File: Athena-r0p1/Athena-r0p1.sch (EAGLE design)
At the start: 30 parts, among them U1 3.3V, U2 AP2127K-1.8V, U3 NCP1117LPST50T3G

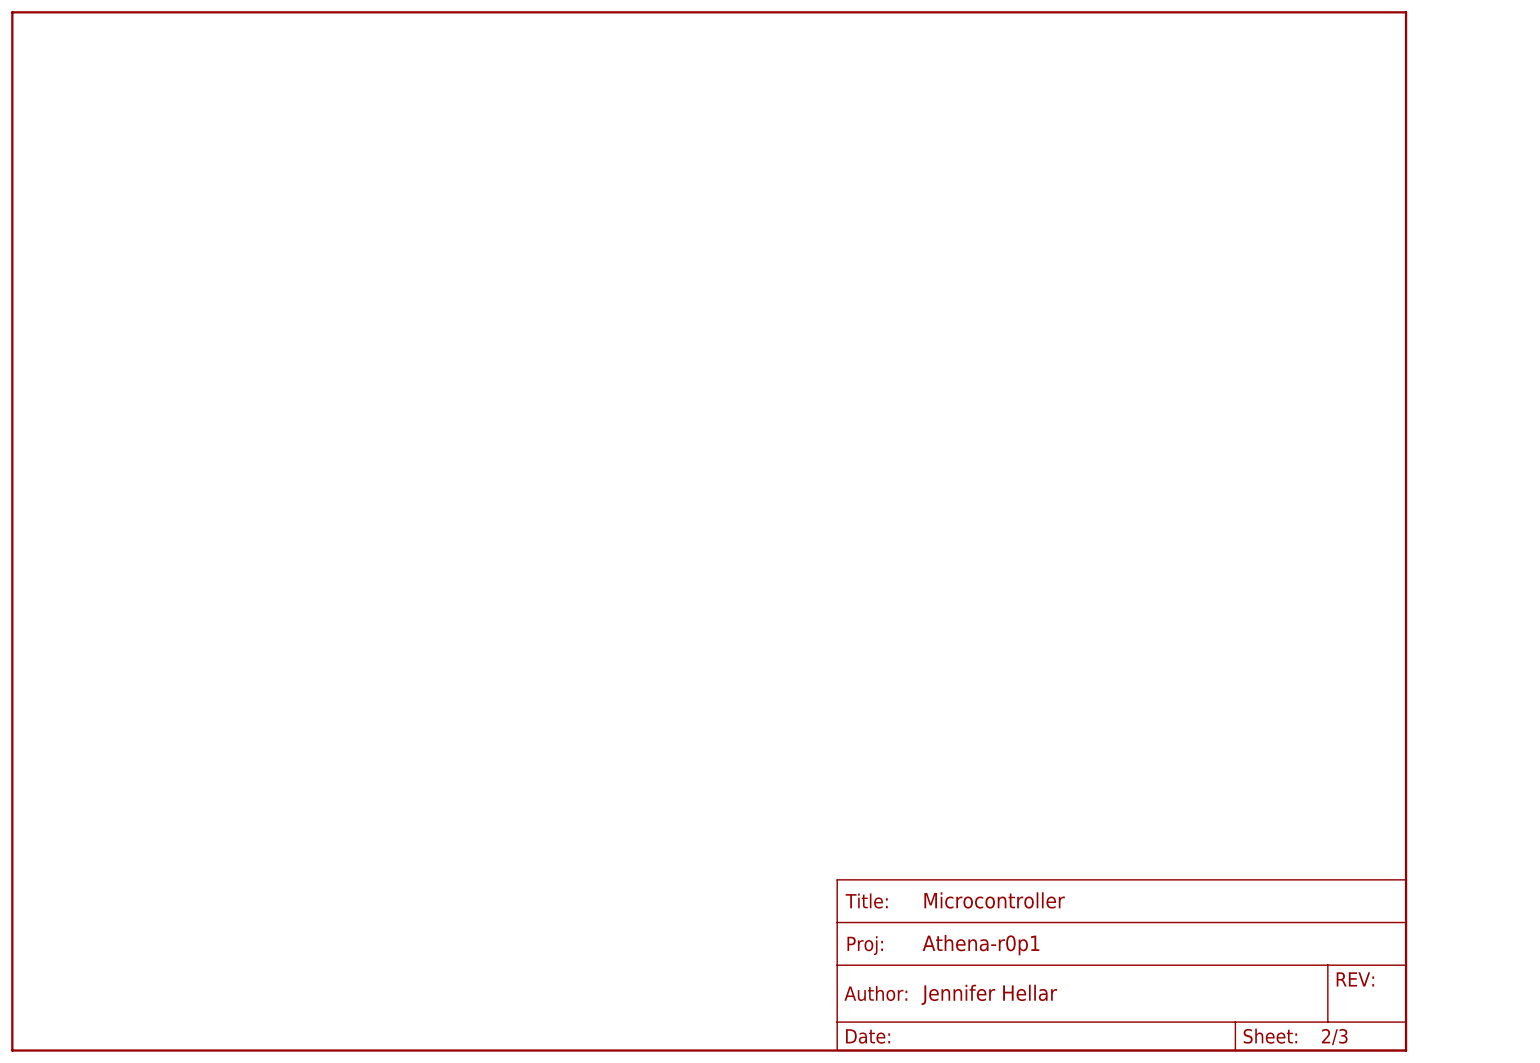
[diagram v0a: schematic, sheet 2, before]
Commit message: Initial work on the MCU portion of the schematic incl. oscillators and flash
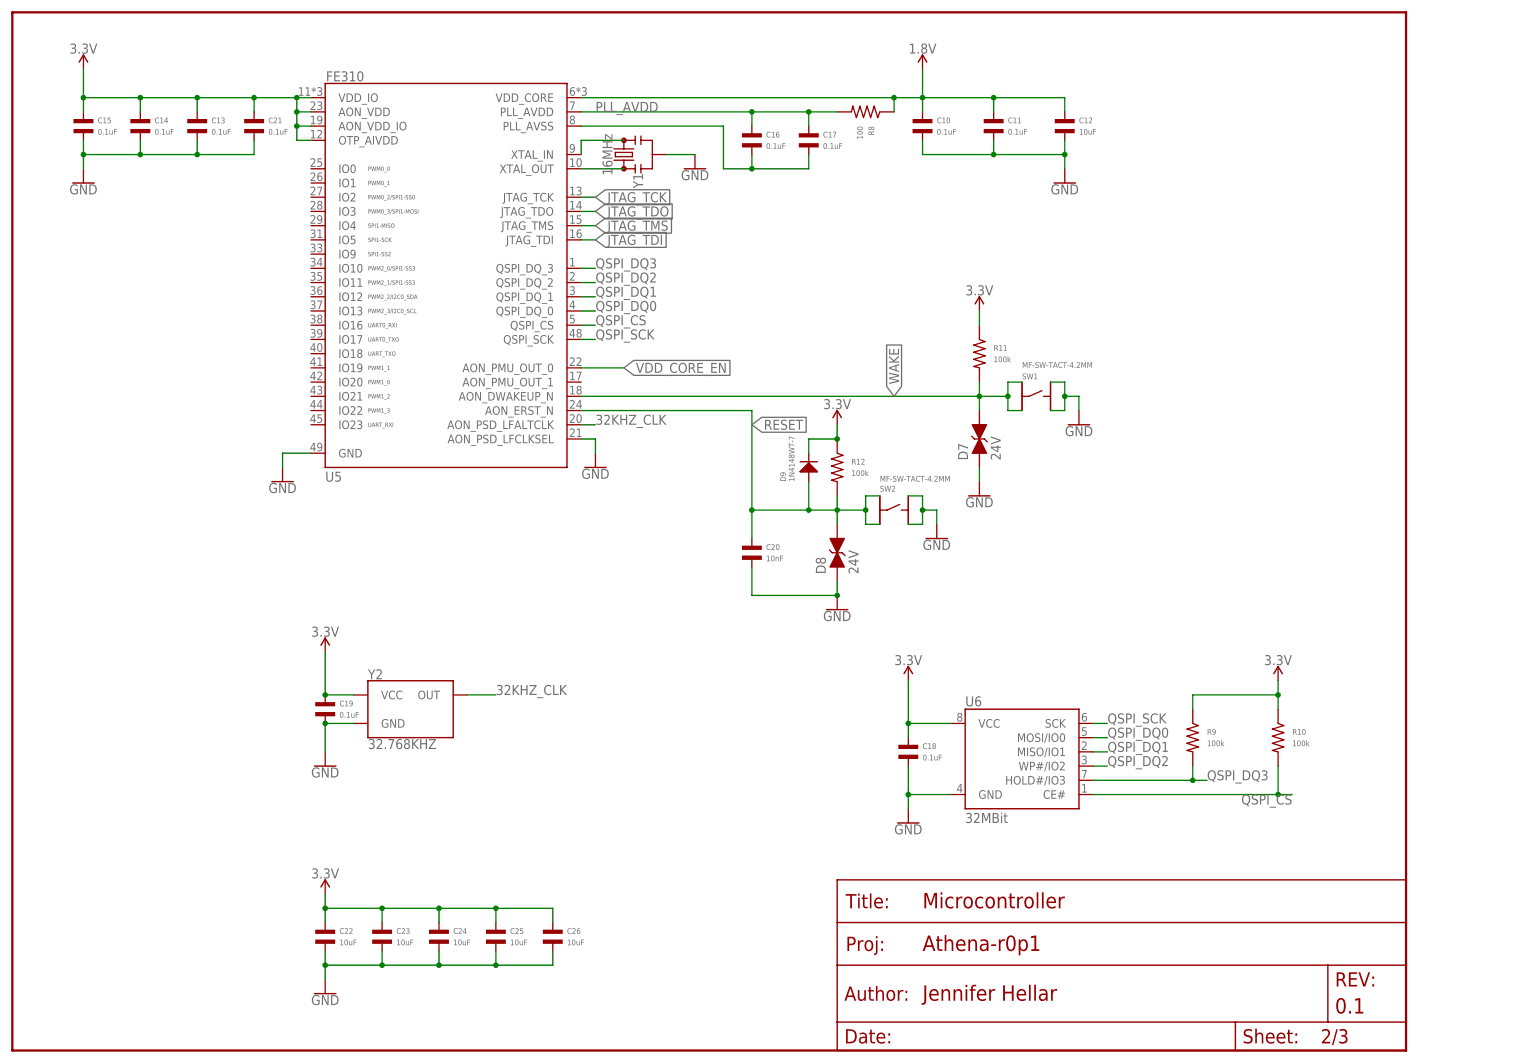
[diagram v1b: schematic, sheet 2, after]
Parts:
- added C10, C11, C13, C14, C15, C16, C17, C18, C19, C21: 0.1uF, MF_Passives:CAPACITOR_NP_0603
- added C12, C22, C23, C24, C25, C26: 10uF, MF_Passives:CAPACITOR_NP_0603
- added C20: 10nF, MF_Passives:CAPACITOR_NP_0603
- added D7, D8: 24V, SparkFun RED-V RedBoard:SPARKFUN-DISCRETESEMI_DIODE_TVS
- added D9: 1N4148WT-7, Athena-r0p1:1N4148WT-7
- added R10, R11, R12, R9: 100k, MF_Passives:RESISTOR_0603
- added R13, R14, R15, R8: 100, MF_Passives:RESISTOR_0603
- added SW1, SW2: MF-SW-TACT-4.2MM, MF_Switches:TACT_4.2MM
- added U5: FE310, Athena-r0p1:IC_MCU_SIFIVE_FE310
- added U6: 32MBit, Athena-r0p1:IC_MEMORY_QSPI32MBIT
- added U7: MK22FN128VLH10, Athena-r0p1:IC_USB_JTAG_MK22FN128VLH10
- added Y1: 16MHz, Athena-r0p1:CLOCK_16MHZ_RESONATORSMD_3.2X1.3
- added Y2: 32.768KHZ, Athena-r0p1:CLOCK_SITIME_CRYSTAL_32.768KHZ
- FRAME1, FRAME2: REV (none) -> 0.1
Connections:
- new net 32KHZ_CLK: U5.AON_PSD_LFALTCLK, Y2.OUT
- new net JTAG_TCK: R14.P$2, U5.JTAG_TCK
- new net JTAG_TDI: R13.P$2, U5.JTAG_TDI
- new net JTAG_TDO: U5.JTAG_TDO, U7.PTE1/LLWU_P0
- new net JTAG_TMS: R15.P$1, U5.JTAG_TMS
- new net N$10: C16.P$2, C17.P$2, U5.PLL_AVSS
- new net N$11: U5.XTAL_OUT, Y1.1
- new net N$12: R13.P$1, U7.PTD2/LLWU_P13
- new net N$14: R14.P$1, U7.PTD5
- new net N$16: R15.P$2, U7.PTD6/LLWU_P15
- new net N$9: U5.XTAL_IN, Y1.3
- new net PLL_AVDD: C16.P$1, C17.P$1, R8.P$2, U5.PLL_AVDD
- new net QSPI_CS: R10.P$2, U5.QSPI_CS, U6.CE#
- new net QSPI_DQ0: U5.QSPI_DQ_0, U6.MOSI/IO0
- new net QSPI_DQ1: U5.QSPI_DQ_1, U6.MISO/IO1
- new net QSPI_DQ2: U5.QSPI_DQ_2, U6.WP#/IO2
- new net QSPI_DQ3: R9.P$2, U5.QSPI_DQ_3, U6.HOLD#/IO3
- new net QSPI_SCK: U5.QSPI_SCK, U6.SCK
- new net RESET: C20.P$1, D8.C, D9.ANODE, R12.P$2, SW2.P$3, SW2.P$4, U5.AON_ERST_N
- new net WAKE: D7.C, R11.P$2, SW1.P$3, SW1.P$4, U5.AON_DWAKEUP_N
- net 1.8V: now also C10.P$1, C11.P$1, C12.P$1, R8.P$1, U5.VDD_CORE
- net 3.3V: now also C13.P$1, C14.P$1, C15.P$1, C18.P$1, C19.P$1, C21.P$1, C22.P$1, C23.P$1, C24.P$1, C25.P$1, C26.P$1, D9.CATHODE, R10.P$1, R11.P$1, R12.P$1, R9.P$1, U5.AON_VDD, U5.AON_VDD_IO, U5.OTP_AIVDD, U5.VDD_IO, U6.VCC, Y2.VCC; no longer C1.P$2, C4.P$2, C5.P$2, C6.P$2, C8.P$2, C9.P$2, D2.CATHODE, D3.CATHODE, D4.CATHODE, R6.P$1, U1.GND, U2.GND, U4.VSS, X1.2
- net GND: now also C1.P$2, C10.P$2, C11.P$2, C12.P$2, C13.P$2, C14.P$2, C15.P$2, C18.P$2, C19.P$2, C20.P$2, C21.P$2, C22.P$2, C23.P$2, C24.P$2, C25.P$2, C26.P$2, C4.P$2, C5.P$2, C6.P$2, C8.P$2, C9.P$2, D2.CATHODE, D3.CATHODE, D4.CATHODE, D7.A, D8.A, R6.P$1, SW1.P$1, SW1.P$2, SW2.P$1, SW2.P$2, U1.GND, U2.GND, U4.VSS, U5.AON_PSD_LFCLKSEL, U5.GND, U6.GND, X1.2, Y1.2, Y2.GND
- net VDD_CORE_EN: now also U5.AON_PMU_OUT_0

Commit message: Initial work on the USB-JTAG portion of Nest.  Added PWR/JTAG header to separate Owl and Nest.  Pdf of RedBoard schematic reference added for ease of viewing
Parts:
- added C27, C28, C29, C30, C32: 0.1uF, MF_Passives:CAPACITOR_NP_0603
- added C31: 10uF, MF_Passives:CAPACITOR_NP_0603
- added FRAME4: FRAME-LETTER, Athena-r0p1:FRAME-LETTER
- added J1: CONN_12X2, SparkFun-Connectors:CONN_12X2
- added J2: MF-CON-MICROUSB-RIGHT, MF_Connectors:USB_MICRO_RIGHT
- added J3-MK22-DBG: FEMALE 2x3, SparkFun-Connectors:CONN_03X2FEMALE
- added R16: 100k, MF_Passives:RESISTOR_0603
- added U8: MIC803-30D2VC3-TR, Athena-r0p1:MIC803-30D2VC3-TR
- FRAME1: SHEETNM Power -> Power (Nest)
- FRAME2: SHEETNM Microcontroller -> Microcontroller (Owl)
- FRAME3: REV (none) -> 0.1; SHEETNM Nest -> USB-JTAG (Nest)
- U1: value 3.3V -> NCP1117-VREG-5V0; device Athena-r0p1:IC_POWER_3.3V_REG_AP2112K-3.3V -> Athena-r0p1:NCP1117LPST50T3G
- U2: value AP2127K-1.8V -> AP2112-VREG-3V3; device Athena-r0p1:IC_POWER_1P8V_REG_AP2127K-1.8V -> Athena-r0p1:IC_POWER_3.3V_REG_AP2112K-3.3V
- U3: value NCP1117LPST50T3G -> AP2127K-VREG-1V8; device Athena-r0p1:NCP1117LPST50T3G -> Athena-r0p1:IC_POWER_1P8V_REG_AP2127K-1.8V
- U4: value (none) -> MCP73831/2
- X1: value (none) -> JST 2-Pin
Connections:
- new net CORE_EN_NEST: J1.24, R2.P$2, R5.P$1
- new net DBG_RESET: J3-MK22-DBG.3, R16.P$1, U7.RESET_B, U8.!RESET
- new net DBG_SWDCLK: J3-MK22-DBG.4, U7.PTA0
- new net DBG_SWDIO: J3-MK22-DBG.2, U7.PTA3
- new net DBG_SWO: J3-MK22-DBG.6, U7.PTA2
- new net JTAG_TCK_NEST: J1.16, R14.P$2
- new net JTAG_TDI_NEST: J1.20, R13.P$2
- new net JTAG_TDO_NEST: J1.18, U7.PTE1/LLWU_P0
- new net JTAG_TMS_NEST: J1.14, R15.P$1
- new net RESET_NEST: J1.22, U7.PTD7
- new net UART_RX: J1.11, U5.IO16
- new net UART_RX_NEST: J1.10, U7.PTB16
- new net UART_TX: J1.9, U5.IO17
- new net UART_TX_NEST: J1.12, U7.PTB17
- new net USB_N: J2.D-, U7.D-
- new net USB_P: J2.D+, U7.D+
- net 1.8V: now also J1.7, J1.8, U3.OUT; no longer U2.OUT
- net 3.3V: now also C27.P$1, C28.P$1, C29.P$1, C30.P$1, C31.P$1, D2.ANODE, J1.5, J1.6, J3-MK22-DBG.1, R16.P$2, U2.OUT, U7.PTA4/LLWU_P3, U7.USBVDD, U7.VBATT, U7.VDD, U7.VDDA, U7.VREFH; no longer R3.P$1, U1.OUT
- net 5V: now also C32.P$1, J1.3, J1.4, U1.OUTPUT, U3.IN, U8.VCC; no longer U1.IN, U3.OUTPUT
- net GND: now also C27.P$2, C28.P$2, C29.P$2, C30.P$2, C31.P$2, C32.P$2, J1.1, J1.2, J2.GND, J2.SLD, J3-MK22-DBG.5, R3.P$2, U1.ADJUST/GROUND, U3.GND, U7.GND, U7.VREFL, U7.VSSA, U8.GND; no longer D2.CATHODE, U1.GND, U3.ADJUST/GROUND
- net JTAG_TCK: now also J1.15; no longer R14.P$2
- net JTAG_TDI: now also J1.19; no longer R13.P$2
- net JTAG_TDO: now also J1.17; no longer U7.PTE1/LLWU_P0
- net JTAG_TMS: now also J1.13; no longer R15.P$1
- net N$2: now also D2.CATHODE, R3.P$1; no longer D2.ANODE, R3.P$2
- net N$3: now also U2.EN; no longer U1.EN
- net N$4: now also U3.EN; no longer U2.EN
- net RESET: now also J1.21
- net VDD_CORE_EN: now also J1.23; no longer R2.P$2, R5.P$1
- net V_USB: now also J2.5V, U1.INPUT; no longer U3.INPUT
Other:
- note added: "Is one pin sufficient for transferring pwr from nest to owl? Or should we double up 3.3V and 1.8V and GND pins to have a stronger connection?"
- note added: "Not sure how to incorporate multiple power sources (V_BATT and V_USB) Also need to choose an actual device for D6"
- note added: "Resistor(s) needed for impedance matching?"

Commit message: Athena Rev. 0.1 Schematic complete.
1. Switched out oscillators to match the parts used in HiFive
2. Cleaned and commented the schematics
3. Completed the header pinout
4. Removed unused parts from the library
5. Added datasheets for all non-passives
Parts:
- removed J1: CONN_12X2, SparkFun-Connectors:CONN_12X2
- removed J2: MF-CON-MICROUSB-RIGHT, MF_Connectors:USB_MICRO_RIGHT
- added C33, C34: 15pF, MF_Passives:CAPACITOR_NP_0603
- added FRAME5: FRAME-LETTER, Athena-r0p1:FRAME-LETTER
- added J1-NEST-OWL1: CONN_12X2, SparkFun-Connectors:CONN_12X2
- added J2-USB: MF-CON-MICROUSB-RIGHT, MF_Connectors:USB_MICRO_RIGHT
- added J4, J5: MF-CON-2.54mm-01x14, MF_Connectors:CON_01X14_PTH_2.54MM
- added R17: 1M, MF_Passives:RESISTOR_0603
- D6: value (none) -> MBR120
- U2: value AP2112-VREG-3V3 -> RT9080-33GJ5; device Athena-r0p1:IC_POWER_3.3V_REG_AP2112K-3.3V -> Athena-r0p1:RT9080-33GJ5
- U3: value AP2127K-VREG-1V8 -> RT9080-18GJ5; device Athena-r0p1:IC_POWER_1P8V_REG_AP2127K-1.8V -> Athena-r0p1:RT9080-18GJ5
- Y1: value 16MHz -> TSX-3225-16.0000MF18X-AC0; device Athena-r0p1:CLOCK_16MHZ_RESONATORSMD_3.2X1.3 -> Athena-r0p1:TSX-3225-16.0000MF18X-AC0
- Y2: value 32.768KHZ -> SIT1533AI-H4-DCC-32.768E; device Athena-r0p1:CLOCK_SITIME_CRYSTAL_32.768KHZ -> Athena-r0p1:SIT1533AI-H4-DCC-32.768E
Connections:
- removed net N$11: U5.XTAL_OUT, Y1.1
- removed net N$9: U5.XTAL_IN, Y1.3
- new net 16MHZ_IN: C33.P$1, R17.P$2, U5.XTAL_IN, Y1.1
- new net 16MHZ_OUT: C34.P$1, R17.P$1, U5.XTAL_OUT, Y1.3
- new net CS0: J4.PIN4, U5.IO2
- new net CS2: J4.PIN8, U5.IO9
- new net CS3: J4.PIN9, U5.IO10
- new net IO11: J4.PIN10, U5.IO11
- new net IO19: J5.PIN7, U5.IO19
- new net IO20: J5.PIN8, U5.IO20
- new net IO21: J5.PIN9, U5.IO21
- new net IO22: J5.PIN10, U5.IO22
- new net MISO: J4.PIN6, U5.IO4
- new net MOSI: J4.PIN5, U5.IO3
- new net PWM0_0: J5.PIN5, U5.IO0
- new net PWM0_1: J5.PIN6, U5.IO1
- new net RXI: J5.PIN12, U5.IO23
- new net SCK: J4.PIN7, U5.IO5
- new net SCL: J4.PIN12, U5.IO13
- new net SDA: J4.PIN11, U5.IO12
- new net TXO: J5.PIN11, U5.IO18
- net 1.8V: now also J1-NEST-OWL1.7, J1-NEST-OWL1.8, U3.VOUT; no longer J1.7, J1.8, U3.OUT
- net 3.3V: now also J1-NEST-OWL1.5, J1-NEST-OWL1.6, J4.PIN14, J4.PIN2, J5.PIN14, U2.VOUT, Y2.VDD; no longer C7.P$2, J1.5, J1.6, U2.OUT, Y2.VCC
- net 32KHZ_CLK: now also Y2.CLK_OUT; no longer Y2.OUT
- net 5V: now also J1-NEST-OWL1.3, J1-NEST-OWL1.4, J4.PIN1, U2.VIN, U3.VIN; no longer J1.3, J1.4, U2.IN, U3.IN
- net CORE_EN_NEST: now also J1-NEST-OWL1.24; no longer J1.24
- net GND: now also C33.P$2, C34.P$2, C7.P$2, J1-NEST-OWL1.1, J1-NEST-OWL1.2, J2-USB.GND, J2-USB.SLD, J4.PIN13, J4.PIN3, J5.PIN13, J5.PIN4, Y1.4; no longer J1.1, J1.2, J2.GND, J2.SLD
- net JTAG_TCK: now also J1-NEST-OWL1.15; no longer J1.15
- net JTAG_TCK_NEST: now also J1-NEST-OWL1.16; no longer J1.16
- net JTAG_TDI: now also J1-NEST-OWL1.19; no longer J1.19
- net JTAG_TDI_NEST: now also J1-NEST-OWL1.20; no longer J1.20
- net JTAG_TDO: now also J1-NEST-OWL1.17; no longer J1.17
- net JTAG_TDO_NEST: now also J1-NEST-OWL1.18; no longer J1.18
- net JTAG_TMS: now also J1-NEST-OWL1.13; no longer J1.13
- net JTAG_TMS_NEST: now also J1-NEST-OWL1.14; no longer J1.14
- net RESET: now also J1-NEST-OWL1.21, J5.PIN1; no longer J1.21
- net RESET_NEST: now also J1-NEST-OWL1.22; no longer J1.22
- net UART_RX: now also J1-NEST-OWL1.11; no longer J1.11
- net UART_RX_NEST: now also J1-NEST-OWL1.10; no longer J1.10
- net UART_TX: now also J1-NEST-OWL1.9; no longer J1.9
- net UART_TX_NEST: now also J1-NEST-OWL1.12; no longer J1.12
- net USB_N: now also J2-USB.D-; no longer J2.D-
- net USB_P: now also J2-USB.D+; no longer J2.D+
- net VDD_CORE_EN: now also J1-NEST-OWL1.23, J5.PIN3; no longer J1.23
- net V_USB: now also J2-USB.5V; no longer J2.5V
- net WAKE: now also J5.PIN2
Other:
- note added: "CONTROL"
- note added: "GPIO"
- note added: "I2C"
- note added: "Not sure how to incorporate multiple power sources (V_BATT and V_USB) Ref. HiFive for NCP1117 circuit"
- note added: "POWER"
- note added: "Ref. Feather for MCP73831 circuit"
- note added: "Ref. HiFive for MK22 circuit"
- note added: "Ref. HiFive for RT9080 circuits"
- note added: "Ref. to HiFive for Flash circuit Prod: IS25LP032D-JBLE"
- note added: "SPI1"
- note added: "UART1"
- note removed: "Not sure how to incorporate multiple power sources (V_BATT and V_USB) Also need to choose an actual device for D6"
